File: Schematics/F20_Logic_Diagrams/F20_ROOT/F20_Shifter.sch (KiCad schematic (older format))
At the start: 2 parts

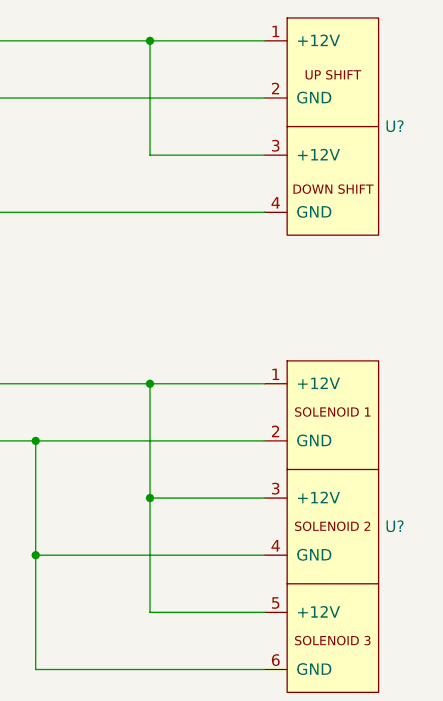
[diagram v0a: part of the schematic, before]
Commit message: Re-annotated Logic Diagrams, pulled a BOM list based on Logic Diagrams
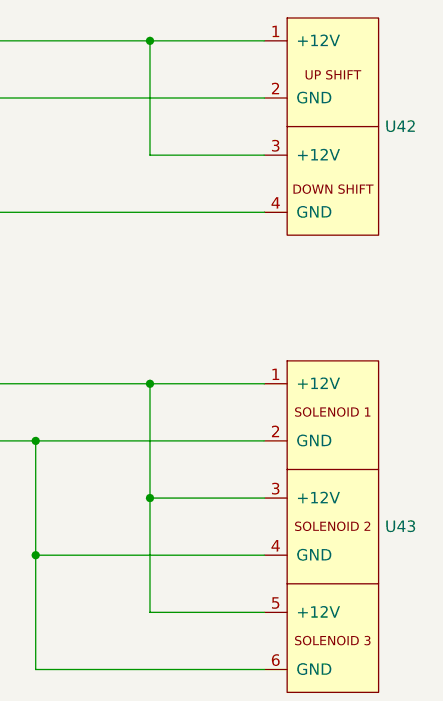
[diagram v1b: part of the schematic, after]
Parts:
- gave numbers to parts that had none: 2
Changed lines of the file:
@@
 $EndDescr
 $Comp
-L FSAE_Library:Up_Down_Shifter U?
+L FSAE_Library:Up_Down_Shifter U42
 U 1 1 5E628367
 P 7500 2000
-F 0 "U?" H 8028 1625 50  0000 L CNN
+F 0 "U42" H 8028 1625 50  0000 L CNN
 F 1 "Up_Down_Shifter" H 7800 2150 50  0001 C CNN
 F 2 "" H 8000 2500 50  0001 C CNN
@@
 $EndComp
 $Comp
-L FSAE_Library:Clutch_Actuator U?
+L FSAE_Library:Clutch_Actuator U43
 U 1 1 5E628FDC
 P 7500 3500
-F 0 "U?" H 8028 2875 50  0000 L CNN
+F 0 "U43" H 8028 2875 50  0000 L CNN
 F 1 "Clutch_Actuator" H 7800 3650 50  0001 C CNN
 F 2 "" H 8000 4000 50  0001 C CNN
